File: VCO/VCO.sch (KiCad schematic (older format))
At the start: 40 parts, among them J101 EuroPower, J102 CV, J103 Square, J104 PWM, J105 CV PWM, J106 Triangle, J107 Ramp, SW101 Octave, U101 TL082

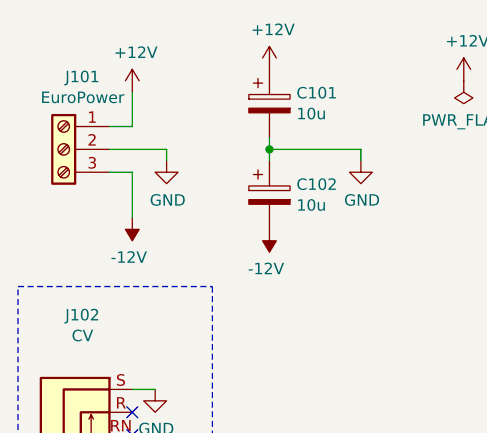
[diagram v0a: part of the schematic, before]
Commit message: Added HF trim, ready to fab
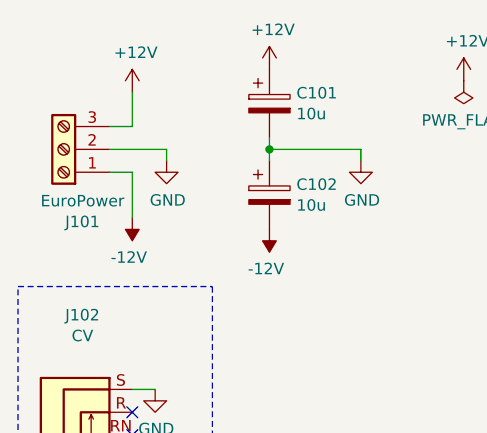
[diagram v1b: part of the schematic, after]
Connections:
- net +12V: now also J101.3 (Pin_3); no longer J101.1 (Pin_1)
- net -12V: now also J101.1 (Pin_1); no longer J101.3 (Pin_3)
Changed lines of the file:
@@
 F 3 "~" H 750 1150 50  0001 C CNN
 	1    750  1150
-	-1   0    0    -1
+	-1   0    0    1
 $EndComp
 Wire Wire Line
